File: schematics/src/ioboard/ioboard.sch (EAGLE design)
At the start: 72 parts, among them IC1 TL072P, IC2 TL072P, IC3 TL072P

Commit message: Updated Schematics, Fixed Power Socket orientation
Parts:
- BD1_TONE, BD1_TUNE, BD2_TUNE: value ALPHA-9MMA -> 50k log
- BD2_DECAY: value ALPHA-9MMA -> 1M log
- C1: value (none) -> 1uF/50v
- C16: value 1u/50v -> 1uF/50v
- C17: value 0.01u -> .01uF
- R2: value (none) -> 220
- R5: value (none) -> 4.7k
- SD_DECAY, SD_NOISE: value ALPHA-9MMA -> 100k lin
- SD_SNAPPY: value ALPHA-9MMA -> 50k lin
- SD_TUNE: value ALPHA-9MMA -> 1k lin
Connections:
- net +12V: now also R26.1
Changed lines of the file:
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@@
 <part name="SD_TRIGGER" library="thonkiconn" deviceset="WQP-PJ301M-12_JACK" device="" value=""/>
 <part name="SD_OUT" library="thonkiconn" deviceset="WQP-PJ301M-12_JACK" device="" value=""/>
-<part name="BD1_TONE" library="TomW" deviceset="ALPHA-9MM" device="A"/>
-<part name="BD1_TUNE" library="TomW" deviceset="ALPHA-9MM" device="A"/>
+<part name="BD1_TONE" library="TomW" deviceset="ALPHA-9MM" device="A" value="50k log"/>
+<part name="BD1_TUNE" library="TomW" deviceset="ALPHA-9MM" device="A" value="50k log"/>
 <part name="BD1_VOLUME" library="TomW" deviceset="ALPHA-9MM" device="A" value="50k log"/>
-<part name="BD2_DECAY" library="TomW" deviceset="ALPHA-9MM" device="A"/>
+<part name="BD2_DECAY" library="TomW" deviceset="ALPHA-9MM" device="A" value="1M log"/>
 <part name="BD2_VOLUME" library="TomW" deviceset="ALPHA-9MM" device="A" value="50k log"/>
-<part name="BD2_TUNE" library="TomW" deviceset="ALPHA-9MM" device="A"/>
-<part name="SD_TUNE" library="TomW" deviceset="ALPHA-9MM" device="A"/>
-<part name="SD_NOISE" library="TomW" deviceset="ALPHA-9MM" device="A"/>
-<part name="SD_SNAPPY" library="TomW" deviceset="ALPHA-9MM" device="A"/>
+<part name="BD2_TUNE" library="TomW" deviceset="ALPHA-9MM" device="A" value="50k log"/>
+<part name="SD_TUNE" library="TomW" deviceset="ALPHA-9MM" device="A" value="1k lin"/>
+<part name="SD_NOISE" library="TomW" deviceset="ALPHA-9MM" device="A" value="100k lin"/>
+<part name="SD_SNAPPY" library="TomW" deviceset="ALPHA-9MM" device="A" value="50k lin"/>
 <part name="GND1" library="supply1" library_urn="urn:adsk.eagle:library:371" deviceset="GND" device=""/>
 <part name="GND2" library="supply1" library_urn="urn:adsk.eagle:library:371" deviceset="GND" device=""/>
@@
 <part name="R4" library="rcl" library_urn="urn:adsk.eagle:library:334" deviceset="R-US_" device="0207/7" package3d_urn="urn:adsk.eagle:package:23493/2" value="1k"/>
 <part name="GND10" library="supply1" library_urn="urn:adsk.eagle:library:371" deviceset="GND" device=""/>
-<part name="R2" library="rcl" library_urn="urn:adsk.eagle:library:334" deviceset="R-US_" device="0207/7" package3d_urn="urn:adsk.eagle:package:23493/2"/>
+<part name="R2" library="rcl" library_urn="urn:adsk.eagle:library:334" deviceset="R-US_" device="0207/7" package3d_urn="urn:adsk.eagle:package:23493/2" value="220"/>
 <part name="BD1_CON" library="pinhead" library_urn="urn:adsk.eagle:library:325" deviceset="PINHD-1X4" device="" package3d_urn="urn:adsk.eagle:package:22407/2"/>
 <part name="GND11" library="supply1" library_urn="urn:adsk.eagle:library:371" deviceset="GND" device=""/>
-<part name="R5" library="rcl" library_urn="urn:adsk.eagle:library:334" deviceset="R-US_" device="0207/7" package3d_urn="urn:adsk.eagle:package:23493/2"/>
-<part name="C1" library="rcl" library_urn="urn:adsk.eagle:library:334" deviceset="CPOL-US" device="E2.5-5" package3d_urn="urn:adsk.eagle:package:23344/1"/>
+<part name="R5" library="rcl" library_urn="urn:adsk.eagle:library:334" deviceset="R-US_" device="0207/7" package3d_urn="urn:adsk.eagle:package:23493/2" value="4.7k"/>
+<part name="C1" library="rcl" library_urn="urn:adsk.eagle:library:334" deviceset="CPOL-US" device="E2.5-5" package3d_urn="urn:adsk.eagle:package:23344/1" value="1uF/50v"/>
 <part name="GND12" library="supply1" library_urn="urn:adsk.eagle:library:371" deviceset="GND" device=""/>
-<part name="SD_DECAY" library="TomW" deviceset="ALPHA-9MM" device="A"/>
+<part name="SD_DECAY" library="TomW" deviceset="ALPHA-9MM" device="A" value="100k lin"/>
 <part name="GND13" library="supply1" library_urn="urn:adsk.eagle:library:371" deviceset="GND" device=""/>
 <part name="SD_CON" library="pinhead" library_urn="urn:adsk.eagle:library:325" deviceset="PINHD-1X7" device="" package3d_urn="urn:adsk.eagle:package:22477/2"/>
@@
 <part name="GND36" library="supply1" library_urn="urn:adsk.eagle:library:371" deviceset="GND" device=""/>
 <part name="GND37" library="supply1" library_urn="urn:adsk.eagle:library:371" deviceset="GND" device=""/>
-<part name="C16" library="rcl" library_urn="urn:adsk.eagle:library:334" deviceset="CPOL-US" device="E2.5-6" package3d_urn="urn:adsk.eagle:package:23349/1" value="1u/50v"/>
-<part name="C17" library="resistor" deviceset="C-EU" device="050-024X044" value="0.01u"/>
+<part name="C16" library="rcl" library_urn="urn:adsk.eagle:library:334" deviceset="CPOL-US" device="E2.5-6" package3d_urn="urn:adsk.eagle:package:23349/1" value="1uF/50v"/>
+<part name="C17" library="resistor" deviceset="C-EU" device="050-024X044" value=".01uF"/>
 <part name="GND38" library="supply1" deviceset="GND" device=""/>
 <part name="OUT_CON" library="pinhead" library_urn="urn:adsk.eagle:library:325" deviceset="PINHD-1X3" device="" package3d_urn="urn:adsk.eagle:package:22458/2"/>
@@
 <wire x1="190.5" y1="27.94" x2="198.12" y2="27.94" width="0.1524" layer="91"/>
 </segment>
-</net>
+<segment>
+<pinref part="R26" gate="G$1" pin="1"/>
+<pinref part="P+5" gate="1" pin="+12V"/>
+<wire x1="317.5" y1="213.36" x2="317.5" y2="210.82" width="0.1524" layer="91"/>
+</segment>
+</net>

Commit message: Some updates & bugfixes
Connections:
- new net N$26: IC3B.OUT, R28.2, SD_VOLUME.E
- net SD_INT_OUT: no longer IC3B.OUT, R28.2, SD_VOLUME.E
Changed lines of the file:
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@@
 </instance>
 <instance part="C1" gate="G$1" x="292.1" y="50.8" smashed="yes">
-<attribute name="NAME" x="293.116" y="51.435" size="1.778" layer="95"/>
+<attribute name="NAME" x="295.656" y="51.435" size="1.778" layer="95"/>
 <attribute name="VALUE" x="293.116" y="46.609" size="1.778" layer="96"/>
 </instance>
@@
 <net name="SD_INT_OUT" class="0">
 <segment>
-<pinref part="SD_VOLUME" gate="G$1" pin="E"/>
-<wire x1="330.2" y1="142.24" x2="330.2" y2="144.78" width="0.1524" layer="91"/>
-<pinref part="IC3" gate="B" pin="OUT"/>
-<wire x1="330.2" y1="144.78" x2="325.12" y2="144.78" width="0.1524" layer="91"/>
-<pinref part="R28" gate="G$1" pin="2"/>
-<wire x1="325.12" y1="144.78" x2="320.04" y2="144.78" width="0.1524" layer="91"/>
-<wire x1="317.5" y1="154.94" x2="325.12" y2="154.94" width="0.1524" layer="91"/>
-<wire x1="325.12" y1="154.94" x2="325.12" y2="144.78" width="0.1524" layer="91"/>
-<junction x="325.12" y="144.78"/>
-</segment>
-<segment>
 <wire x1="157.48" y1="25.4" x2="129.54" y2="25.4" width="0.1524" layer="91"/>
 <label x="129.54" y="25.4" size="1.778" layer="95" rot="R180" xref="yes"/>
@@
 </segment>
 </net>
+<net name="N$26" class="0">
+<segment>
+<pinref part="IC3" gate="B" pin="OUT"/>
+<wire x1="320.04" y1="144.78" x2="325.12" y2="144.78" width="0.1524" layer="91"/>
+<pinref part="SD_VOLUME" gate="G$1" pin="E"/>
+<wire x1="325.12" y1="144.78" x2="330.2" y2="144.78" width="0.1524" layer="91"/>
+<wire x1="330.2" y1="144.78" x2="330.2" y2="142.24" width="0.1524" layer="91"/>
+<pinref part="R28" gate="G$1" pin="2"/>
+<wire x1="317.5" y1="154.94" x2="325.12" y2="154.94" width="0.1524" layer="91"/>
+<wire x1="325.12" y1="154.94" x2="325.12" y2="144.78" width="0.1524" layer="91"/>
+<junction x="325.12" y="144.78"/>
+</segment>
+</net>

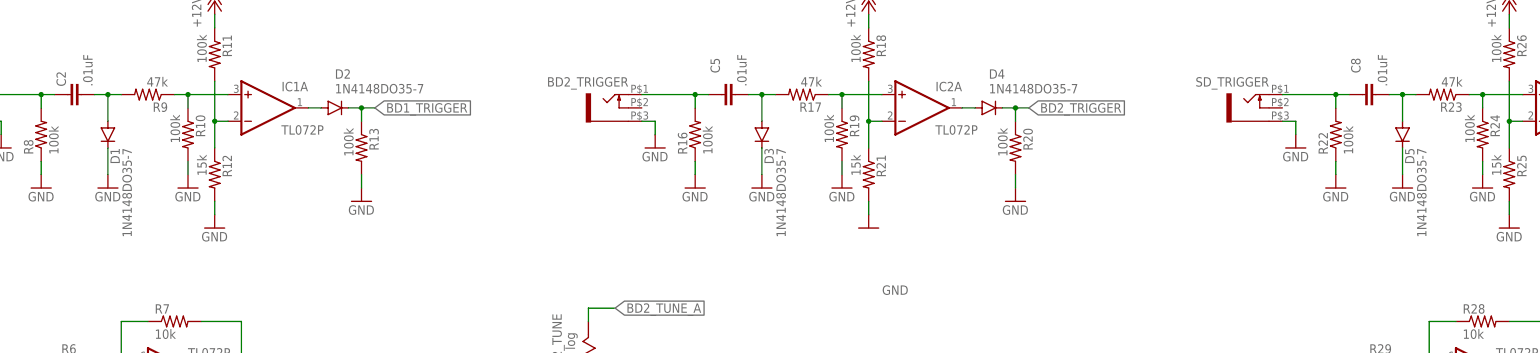
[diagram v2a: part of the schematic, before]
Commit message: Fixed schematics & descriptions
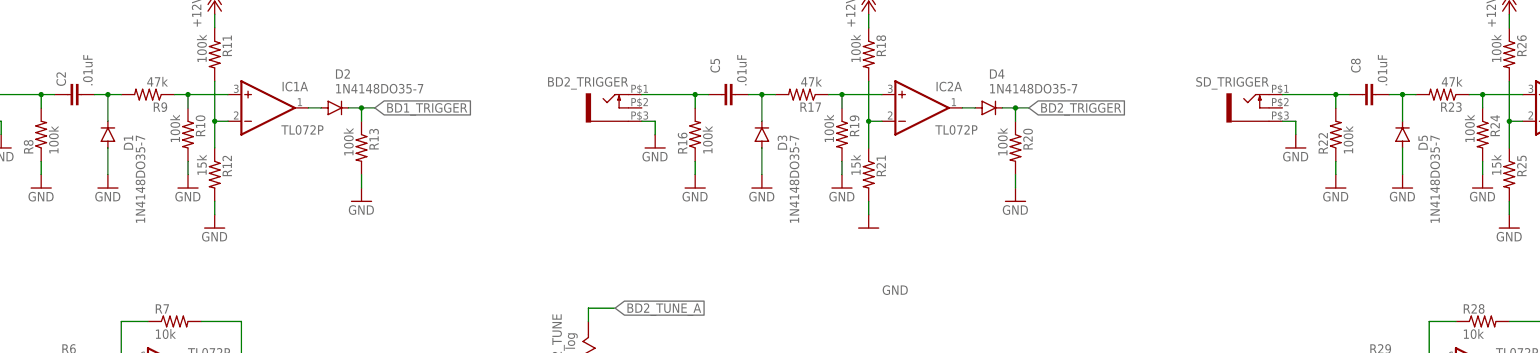
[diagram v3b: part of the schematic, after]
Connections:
- net GND: now also D1.A, D3.A, D5.A; no longer D1.C, D3.C, D5.C
- net N$16: now also D3.C; no longer D3.A
- net N$22: now also D5.C; no longer D5.A
- net N$9: now also D1.C; no longer D1.A
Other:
- moved on the sheet: D1, D3, D5
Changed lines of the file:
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@@
 <attribute name="VALUE" x="62.738" y="194.31" size="1.778" layer="96" rot="R270"/>
 </instance>
-<instance part="D1" gate="G$1" x="50.8" y="190.5" smashed="yes" rot="R270">
-<attribute name="NAME" x="51.2826" y="187.96" size="1.778" layer="95" rot="R270"/>
-<attribute name="VALUE" x="53.5686" y="187.96" size="1.778" layer="96" rot="R270"/>
+<instance part="D1" gate="G$1" x="50.8" y="190.5" smashed="yes" rot="R90">
+<attribute name="NAME" x="53.8226" y="190.5" size="1.778" layer="95" rot="R270"/>
+<attribute name="VALUE" x="56.1086" y="190.5" size="1.778" layer="96" rot="R270"/>
 </instance>
 <instance part="GND15" gate="1" x="38.1" y="180.34" smashed="yes">
@@
 <attribute name="VALUE" x="172.339" y="199.644" size="1.778" layer="96" rot="R90"/>
 </instance>
-<instance part="D3" gate="G$1" x="175.26" y="190.5" smashed="yes" rot="R270">
-<attribute name="NAME" x="175.7426" y="187.96" size="1.778" layer="95" rot="R270"/>
-<attribute name="VALUE" x="178.0286" y="187.96" size="1.778" layer="96" rot="R270"/>
+<instance part="D3" gate="G$1" x="175.26" y="190.5" smashed="yes" rot="R90">
+<attribute name="NAME" x="178.2826" y="190.5" size="1.778" layer="95" rot="R270"/>
+<attribute name="VALUE" x="180.5686" y="190.5" size="1.778" layer="96" rot="R270"/>
 </instance>
 <instance part="R17" gate="G$1" x="182.88" y="198.12" smashed="yes" rot="R180">
@@
 <attribute name="VALUE" x="281.94" y="177.8" size="1.778" layer="96"/>
 </instance>
-<instance part="D5" gate="G$1" x="297.18" y="190.5" smashed="yes" rot="R270">
-<attribute name="NAME" x="297.6626" y="187.96" size="1.778" layer="95" rot="R270"/>
-<attribute name="VALUE" x="299.9486" y="187.96" size="1.778" layer="96" rot="R270"/>
+<instance part="D5" gate="G$1" x="297.18" y="190.5" smashed="yes" rot="R90">
+<attribute name="NAME" x="300.2026" y="190.5" size="1.778" layer="95" rot="R270"/>
+<attribute name="VALUE" x="302.4886" y="190.5" size="1.778" layer="96" rot="R270"/>
 </instance>
 <instance part="C8" gate="G$1" x="289.56" y="198.12" smashed="yes" rot="R90">
@@
 </segment>
 <segment>
-<pinref part="D1" gate="G$1" pin="C"/>
-<pinref part="GND16" gate="1" pin="GND"/>
-<wire x1="50.8" y1="182.88" x2="50.8" y2="187.96" width="0.1524" layer="91"/>
-</segment>
-<segment>
 <pinref part="R10" gate="G$1" pin="2"/>
 <pinref part="GND17" gate="1" pin="GND"/>
@@
 </segment>
 <segment>
-<pinref part="D3" gate="G$1" pin="C"/>
-<pinref part="GND26" gate="1" pin="GND"/>
-<wire x1="175.26" y1="187.96" x2="175.26" y2="182.88" width="0.1524" layer="91"/>
-</segment>
-<segment>
 <pinref part="R20" gate="G$1" pin="2"/>
 <pinref part="GND27" gate="1" pin="GND"/>
@@
 </segment>
 <segment>
-<pinref part="GND32" gate="1" pin="GND"/>
-<pinref part="D5" gate="G$1" pin="C"/>
-<wire x1="297.18" y1="182.88" x2="297.18" y2="187.96" width="0.1524" layer="91"/>
-</segment>
-<segment>
 <pinref part="GND33" gate="1" pin="GND"/>
 <pinref part="R24" gate="G$1" pin="2"/>
@@
 <pinref part="GND39" gate="1" pin="GND"/>
 <wire x1="182.88" y1="25.4" x2="182.88" y2="15.24" width="0.1524" layer="91"/>
+</segment>
+<segment>
+<pinref part="GND26" gate="1" pin="GND"/>
+<pinref part="D3" gate="G$1" pin="A"/>
+<wire x1="175.26" y1="182.88" x2="175.26" y2="187.96" width="0.1524" layer="91"/>
+</segment>
+<segment>
+<pinref part="GND32" gate="1" pin="GND"/>
+<pinref part="D5" gate="G$1" pin="A"/>
+<wire x1="297.18" y1="182.88" x2="297.18" y2="187.96" width="0.1524" layer="91"/>
+</segment>
+<segment>
+<pinref part="GND16" gate="1" pin="GND"/>
+<pinref part="D1" gate="G$1" pin="A"/>
+<wire x1="50.8" y1="182.88" x2="50.8" y2="187.96" width="0.1524" layer="91"/>
 </segment>
 </net>
@@
 <segment>
 <pinref part="C2" gate="G$1" pin="2"/>
-<wire x1="48.26" y1="198.12" x2="50.8" y2="198.12" width="0.1524" layer="91"/>
-<pinref part="D1" gate="G$1" pin="A"/>
-<wire x1="50.8" y1="198.12" x2="50.8" y2="193.04" width="0.1524" layer="91"/>
 <pinref part="R9" gate="G$1" pin="2"/>
 <wire x1="53.34" y1="198.12" x2="50.8" y2="198.12" width="0.1524" layer="91"/>
+<pinref part="D1" gate="G$1" pin="C"/>
+<wire x1="50.8" y1="198.12" x2="48.26" y2="198.12" width="0.1524" layer="91"/>
+<wire x1="50.8" y1="193.04" x2="50.8" y2="198.12" width="0.1524" layer="91"/>
 <junction x="50.8" y="198.12"/>
 </segment>
@@
 <pinref part="R17" gate="G$1" pin="2"/>
 <wire x1="177.8" y1="198.12" x2="175.26" y2="198.12" width="0.1524" layer="91"/>
-<pinref part="D3" gate="G$1" pin="A"/>
+<pinref part="D3" gate="G$1" pin="C"/>
 <wire x1="175.26" y1="198.12" x2="172.72" y2="198.12" width="0.1524" layer="91"/>
 <wire x1="175.26" y1="193.04" x2="175.26" y2="198.12" width="0.1524" layer="91"/>
@@
 <pinref part="R23" gate="G$1" pin="2"/>
 <wire x1="294.64" y1="198.12" x2="297.18" y2="198.12" width="0.1524" layer="91"/>
-<pinref part="D5" gate="G$1" pin="A"/>
+<pinref part="D5" gate="G$1" pin="C"/>
 <wire x1="297.18" y1="198.12" x2="299.72" y2="198.12" width="0.1524" layer="91"/>
 <wire x1="297.18" y1="193.04" x2="297.18" y2="198.12" width="0.1524" layer="91"/>

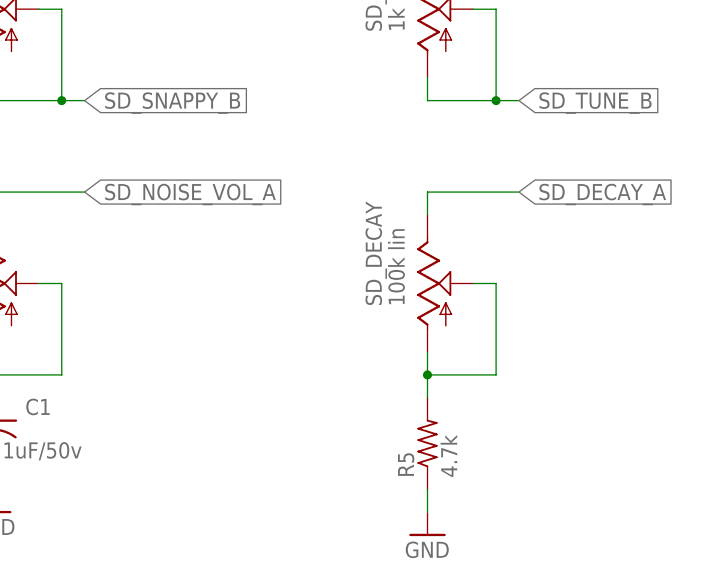
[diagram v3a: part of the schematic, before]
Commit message: Fixed orentation SD Decay pot
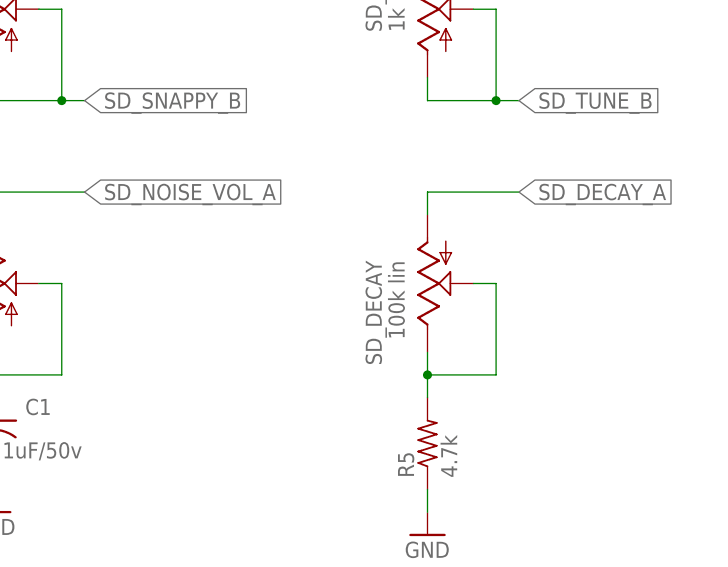
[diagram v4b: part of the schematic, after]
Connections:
- net N$7: now also SD_DECAY.E; no longer SD_DECAY.A
- net SD_DECAY_A: now also SD_DECAY.A; no longer SD_DECAY.E
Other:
- moved on the sheet: SD_DECAY
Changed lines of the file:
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@@
 <attribute name="VALUE" x="289.56" y="38.1" size="1.778" layer="96"/>
 </instance>
-<instance part="SD_DECAY" gate="G$1" x="340.36" y="66.04" smashed="yes">
-<attribute name="NAME" x="335.28" y="63.5" size="1.778" layer="95" rot="R90"/>
-<attribute name="VALUE" x="337.82" y="63.5" size="1.778" layer="96" rot="R90"/>
+<instance part="SD_DECAY" gate="G$1" x="340.36" y="66.04" smashed="yes" rot="MR180">
+<attribute name="NAME" x="335.28" y="68.58" size="1.778" layer="95" rot="MR270"/>
+<attribute name="VALUE" x="337.82" y="68.58" size="1.778" layer="96" rot="MR270"/>
 </instance>
 <instance part="GND13" gate="1" x="340.36" y="38.1" smashed="yes">
@@
 <net name="SD_DECAY_A" class="0">
 <segment>
-<pinref part="SD_DECAY" gate="G$1" pin="E"/>
-<wire x1="340.36" y1="73.66" x2="340.36" y2="76.2" width="0.1524" layer="91"/>
 <wire x1="340.36" y1="76.2" x2="350.52" y2="76.2" width="0.1524" layer="91"/>
 <label x="350.52" y="76.2" size="1.778" layer="95" xref="yes"/>
+<pinref part="SD_DECAY" gate="G$1" pin="A"/>
+<wire x1="340.36" y1="73.66" x2="340.36" y2="76.2" width="0.1524" layer="91"/>
 </segment>
 <segment>
@@
 <net name="N$7" class="0">
 <segment>
-<pinref part="SD_DECAY" gate="G$1" pin="A"/>
-<wire x1="340.36" y1="58.42" x2="340.36" y2="55.88" width="0.1524" layer="91"/>
 <wire x1="340.36" y1="53.34" x2="340.36" y2="55.88" width="0.1524" layer="91"/>
 <wire x1="340.36" y1="55.88" x2="347.98" y2="55.88" width="0.1524" layer="91"/>
 <wire x1="347.98" y1="55.88" x2="347.98" y2="66.04" width="0.1524" layer="91"/>
+<pinref part="R5" gate="G$1" pin="2"/>
+<pinref part="SD_DECAY" gate="G$1" pin="E"/>
+<wire x1="340.36" y1="55.88" x2="340.36" y2="58.42" width="0.1524" layer="91"/>
+<junction x="340.36" y="55.88"/>
 <pinref part="SD_DECAY" gate="G$1" pin="S"/>
 <wire x1="347.98" y1="66.04" x2="345.44" y2="66.04" width="0.1524" layer="91"/>
-<junction x="340.36" y="55.88"/>
-<pinref part="R5" gate="G$1" pin="2"/>
-</segment>
-</net>
+</segment>
+</net>
